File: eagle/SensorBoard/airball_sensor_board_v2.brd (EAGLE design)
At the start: 139.7 x 38.1 mm, 33 parts, among them U2 TMP102

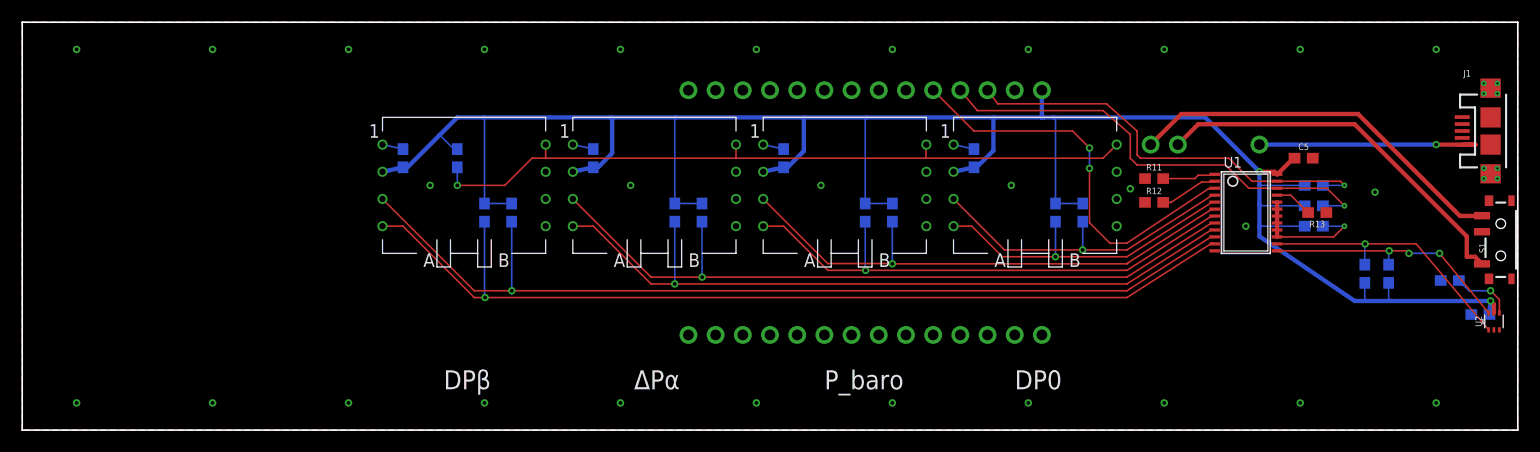
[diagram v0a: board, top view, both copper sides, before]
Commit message: Added airball sensor board v2; renames and cleanups of EAGLE files
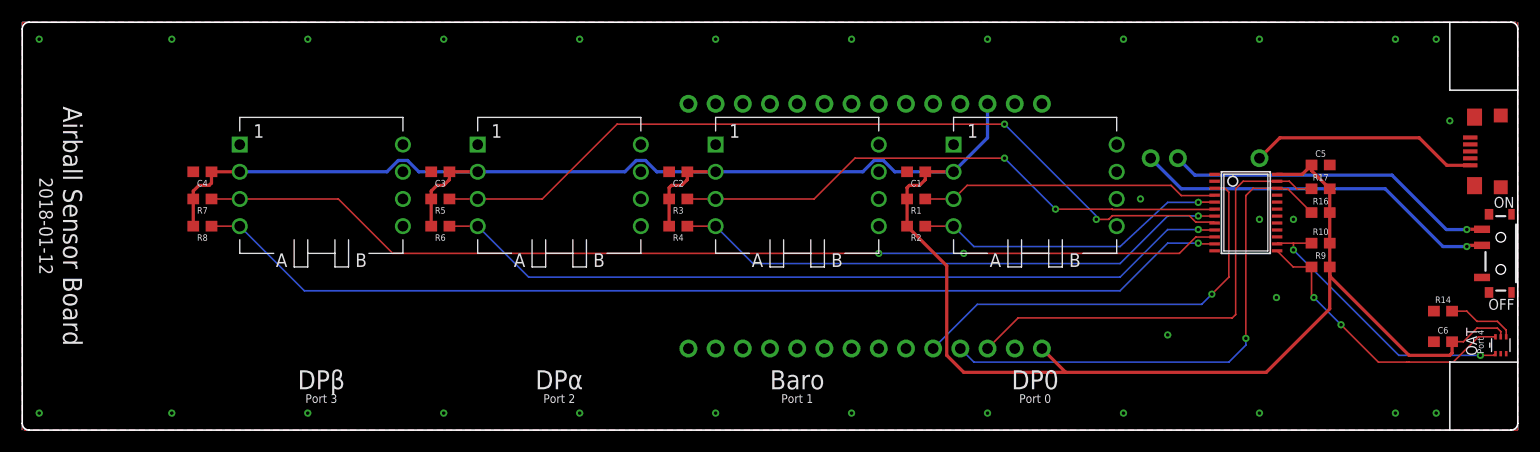
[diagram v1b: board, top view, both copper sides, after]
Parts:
- removed J1: (no value), SparkFun-Connectors:USB-MICROB
- removed R11, R12, R13, R15, R20: 4.7k, SparkFun-Resistors:0603
- removed U2: TMP102, SparkFun-Sensors:SOT563
- removed UP2, UP3, UP4: (no value), microbuilder:ALL_SENSORS_E1BD_8PIN_THRU
- added BARO, DPA, DPB: (no value), microbuilder:ALL_SENSORS_E1BD_8PIN_THRU
- added JP1: USB_MICROB_PLUG, jcole:USB_MICRO_B_TYCO
- added OAT: TMP102, SparkFun-Sensors:SOT563
- C1, C2, C3, C4, C5, C6: value 4.7uF -> 0.1uF
- moved R7 28.9 mm to (16.8, 21.6), flipped to the top, turned to 180 degrees
- moved R8 26.4 mm to (16.8, 19.1), flipped to the top, turned to 180 degrees
- moved R5 24.5 mm to (39.1, 21.6), flipped to the top, turned to 180 degrees
- moved R6 21.9 mm to (39.1, 19.1), flipped to the top, turned to 180 degrees
- moved R3 20.0 mm to (61.3, 21.6), flipped to the top, turned to 180 degrees
- moved C4 18.8 mm to (16.8, 24.1), flipped to the top, turned to 180 degrees
- moved R4 17.5 mm to (61.3, 19.1), flipped to the top, turned to 180 degrees
- moved R1 15.6 mm to (83.5, 21.6), flipped to the top, turned to 180 degrees
- moved C3 14.3 mm to (39.1, 24.1), flipped to the top, turned to 180 degrees
- moved R2 13.1 mm to (83.5, 19.1), flipped to the top, turned to 180 degrees
- moved C2 9.92 mm to (61.3, 24.1), flipped to the top, turned to 180 degrees
- moved R9 6.38 mm to (121.3, 15.2), flipped to the top, turned to 0 degrees
- moved C1 5.54 mm to (83.5, 24.1), flipped to the top, turned to 180 degrees
- moved R10 5.02 mm to (121.3, 17.5), flipped to the top, turned to 0 degrees
- moved C6 4.32 mm to (132.7, 8.26), flipped to the top, turned to 180 degrees
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- renumbered UP1 to DP0
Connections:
- removed net #I2C_RST: U$2.P$5, U1.3
- removed net N$1: DP0.P$3, R1.1, U1.4
- removed net N$10: J1.VBUS, U$2.P$31
- removed net N$12: R13.2, U1.21
- removed net N$13: R12.2, U1.2
- removed net N$14: R11.2, U1.1
- removed net N$15: DP0.P$8, R20.1, UP2.P$8, UP3.P$8, UP4.P$8
- removed net N$16: R9.1, U1.13, U2.6
- removed net N$17: R10.1, U1.14, U2.1
- removed net N$18: S1.2, S1.3, U$2.P$30
- removed net N$19: R14.2, U2.4
- removed net N$2: DP0.P$4, R2.1, U1.5
- removed net N$28: R15.1, U1.15, U1.16, U1.17, U1.18, U1.19, U1.20
- removed net N$3: R3.1, U1.6, UP2.P$3
- removed net N$4: R4.1, U1.7, UP2.P$4
- removed net N$5: R5.1, U1.8, UP3.P$3
- removed net N$6: R6.1, U1.9, UP3.P$4
- removed net N$7: R7.1, U1.10, UP4.P$3
- removed net N$8: R8.1, U1.11, UP4.P$4
- removed net N$9: S1.1, U$2.P$29
- removed net SCL_IN: R16.1, U$2.P$4, U1.22
- removed net SDA_IN: R17.1, U$2.P$3, U1.23
- removed net VCC: C1.1, C2.1, C3.1, C4.1, C5.1, C6.1, DP0.P$2, R1.2, R10.2, R15.2, R16.2, R17.2, R2.2, R20.2, R3.2, R4.2, R5.2, R6.2, R7.2, R8.2, R9.2, U$2.P$1, U$2.P$26, U1.24, U2.5, UP2.P$2, UP3.P$2, UP4.P$2
- new net MUX_RST: U$2.D4, U1.3
- new net MUX_SCL: R16.1, U$2.D3, U1.22
- new net MUX_SDA: R17.1, U$2.D2, U1.23
- new net OAT_ADD0: OAT.4, R14.2
- new net SCL_BARO: BARO.SCL_SCK, R4.1, U1.7
- new net SCL_DP0: DP0.SCL_SCK, R2.1, U1.5
- new net SCL_DPA: DPA.SCL_SCK, R6.1, U1.9
- new net SCL_DPB: DPB.SCL_SCK, R8.1, U1.11
- new net SCL_OAT: OAT.1, R10.1, U1.14
- new net SDA_BARO: BARO.SDA_MOSI, R3.1, U1.6
- new net SDA_DP0: DP0.SDA_MOSI, R1.1, U1.4
- new net SDA_DPA: DPA.SDA_MOSI, R5.1, U1.8
- new net SDA_DPB: DPB.SDA_MOSI, R7.1, U1.10
- new net SDA_OAT: OAT.6, R9.1, U1.13
- new net SWA: S1.1, U$2.SWA
- new net SWB: S1.2, U$2.SWB
- new net VCC_3V3: BARO.VS, C1.1, C2.1, C3.1, C4.1, C5.1, C6.1, DP0.VS, DPA.VS, DPB.VS, OAT.5, R1.2, R10.2, R16.2, R17.2, R2.2, R3.2, R4.2, R5.2, R6.2, R7.2, R8.2, R9.2, U$2.VCC_3V3@1, U$2.VCC_3V3@2, U1.24
- new net VCC_USB: JP1.1, U$2.VCC_5V0
- net GND: now also BARO.GND, DP0.GND, DPA.GND, DPB.GND, JP1.5, JP1.SH@1, JP1.SH@2, JP1.SH@3, JP1.SH@4, OAT.2, U$2.GND@1, U$2.GND@2, U1.1, U1.2, U1.21; no longer DP0.P$1, J1.GND, R11.1, R12.1, R13.1, U$2.P$2, U$2.P$28, U2.2, UP2.P$1, UP3.P$1, UP4.P$1
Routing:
- net VCC: track 208.5 -> 0.00 mm, vias 2 -> 0
- net VCC_3V3: track 0.00 -> 208.3 mm
- net SCL_DPB: track 0.00 -> 98.1 mm, vias 0 -> 1
- net SDA_DPB: track 0.00 -> 96.4 mm, vias 0 -> 2
- net N$7: track 89.6 -> 0.00 mm, vias 1 -> 0
- net N$8: track 89.1 -> 0.00 mm, vias 1 -> 0
- net SDA_DPA: track 0.00 -> 78.7 mm, vias 0 -> 2
- net SCL_DPA: track 0.00 -> 75.3 mm, vias 0 -> 1
- net N$5: track 69.6 -> 0.00 mm, vias 1 -> 0
- net N$6: track 69.5 -> 0.00 mm, vias 1 -> 0
- net N$15: track 68.7 -> 0.00 mm, vias 1 -> 0
- net SDA_BARO: track 0.00 -> 52.8 mm, vias 0 -> 2
- net SCL_BARO: track 0.00 -> 52.5 mm, vias 0 -> 1
- net N$3: track 50.2 -> 0.00 mm, vias 1 -> 0
- net N$4: track 49.9 -> 0.00 mm, vias 1 -> 0
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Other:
- outline, holes or cut-outs redrawn
- board text added: "2018-01-12"
- board text added: "3V3"
- board text added: "A0"
- board text added: "A1"
- board text added: "A2"
- board text added: "A3"
- board text added: "A4"
- board text added: "A5"
- board text added: "AREF"
- board text added: "Airball Sensor Board"
- board text added: "Baro"
- board text added: "Battery 1000 mAh LiPo"
- board text added: "D10"
- board text added: "D11"
- board text added: "D14"
- board text added: "D16"
- board text added: "D17"
- board text added: "D2"
- board text added: "D3"
- board text added: "D4"
- board text added: "D5"
- board text added: "D6"
- board text added: "D7"
- board text added: "D8"
- board text added: "D9"
- board text added: "DPα"
- board text added: "GND"
- board text added: "OAT"
- board text added: "OFF"
- board text added: "ON"
- board text added: "Port 0"
- board text added: "Port 1"
- board text added: "Port 2"
- board text added: "Port 3"
- board text added: "Port 4"
- board text added: "RST"
- board text added: "RXI"
- board text added: "SWA"
- board text added: "SWB"
- board text added: "TXO"
- board text added: "USB 5V0"
- board text removed: "BATTERY 1000 mAH LiPo"
- board text removed: "P_baro"
- board text removed: "ΔPα"
